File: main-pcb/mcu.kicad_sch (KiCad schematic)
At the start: 68 parts, among them J4 CORTEX_DEBUG_ETM, J5 CONN_01X03, U1 XC7S100-1FGGA484C, U12 AT24MAC402, U13 ECS-1612MV-250-CN, U14 STM32H735-UFBGA176-25, U15 S27KL0642GABHB020, U16 ECS-1612MV-250-CN

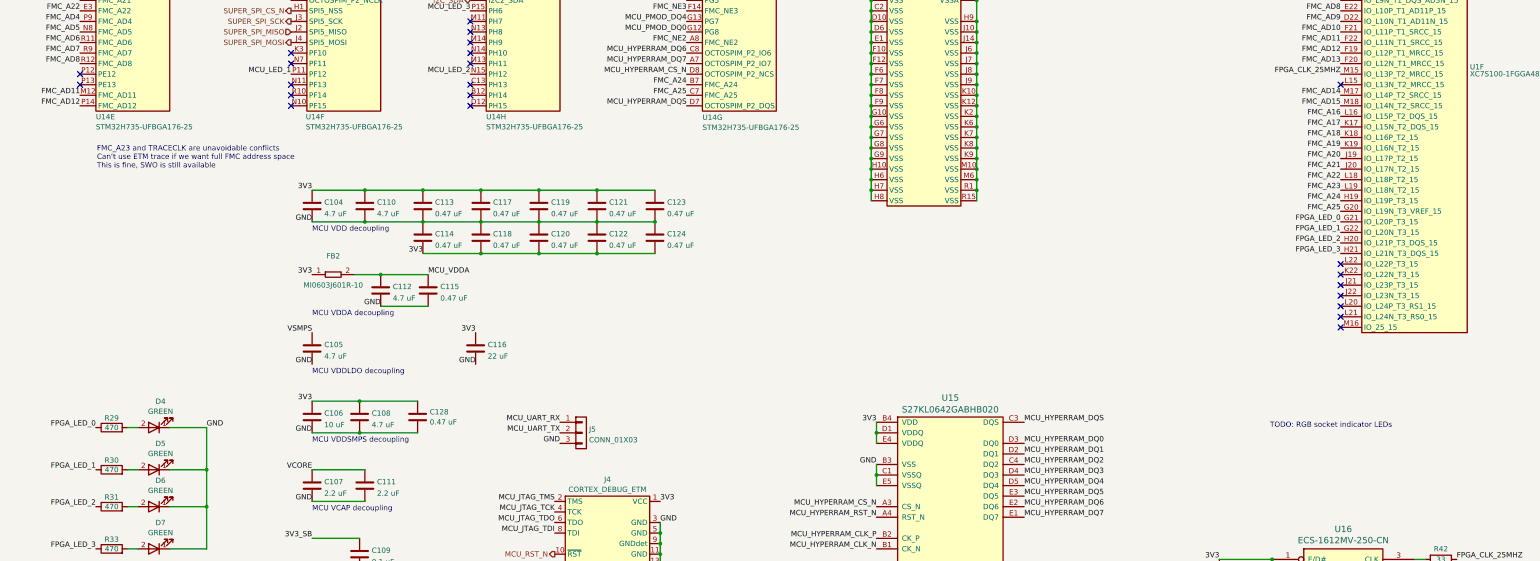
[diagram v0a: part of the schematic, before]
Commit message: Initial design mostly done aside from USB connector, review, test points
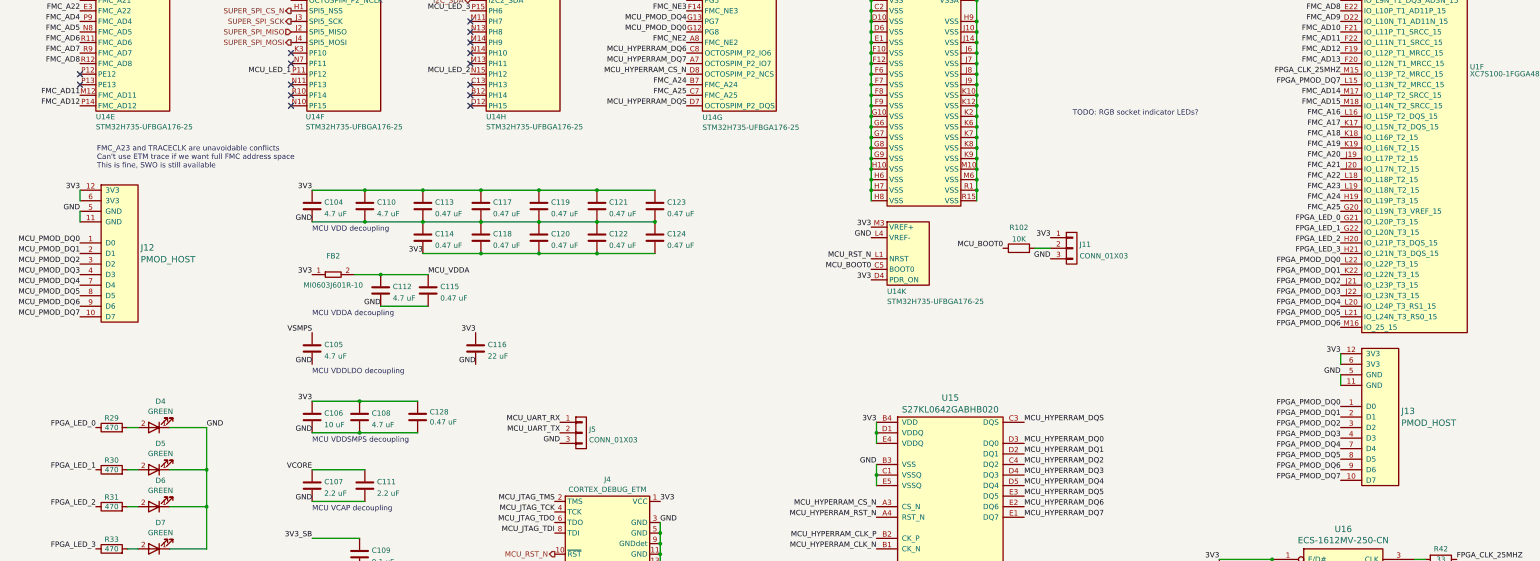
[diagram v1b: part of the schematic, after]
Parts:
- added J11: CONN_01X03, azonenberg_pcb:CONN_HEADER_2.54MM_1x3, symbol conn:CONN_01X03
- added J12, J13: PMOD_HOST, azonenberg_pcb:CONN_HEADER_2.54MM_2x6_RA_PMOD_HOST, symbol special-azonenberg:PMOD_HOST
- added R102: 10K, azonenberg_pcb:EIA_0402_RES_NOSILK, symbol device:R
- added unit 11 of U14
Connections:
- net 3V3: now also J11.1 (P1), J12.12 (3V3), J12.6 (3V3), J13.12 (3V3), J13.6 (3V3), U14.D4 (PDR_ON), U14.M3 (VREF+)
- net GND: now also J11.3 (P3), J12.11 (GND), J12.5 (GND), J13.11 (GND), J13.5 (GND), U14.L4 (VREF-)
- net MCU_PMOD_DQ0: now also J12.1 (D0)
- net MCU_PMOD_DQ1: now also J12.2 (D1)
- net MCU_PMOD_DQ2: now also J12.3 (D2)
- net MCU_PMOD_DQ3: now also J12.4 (D3)
- net MCU_PMOD_DQ4: now also J12.7 (D4)
- net MCU_PMOD_DQ5: now also J12.8 (D5)
- net MCU_PMOD_DQ6: now also J12.9 (D6)
- net MCU_PMOD_DQ7: now also J12.10 (D7)
- net MCU_RST_N: now also U14.L1 (NRST)
- net FPGA_PMOD_DQ2: now reaches U1.J21 (IO_L23P_T3_15)
- net FPGA_PMOD_DQ2: now also J13.3 (D2)
- net FPGA_PMOD_DQ3: now reaches U1.J22 (IO_L23N_T3_15)
- net FPGA_PMOD_DQ3: now also J13.4 (D3)
- net FPGA_PMOD_DQ1: now reaches U1.K22 (IO_L22N_T3_15)
- net FPGA_PMOD_DQ1: now also J13.2 (D1)
- net FPGA_PMOD_DQ7: now reaches U1.L15 (IO_L13N_T2_MRCC_15)
- net FPGA_PMOD_DQ7: now also J13.10 (D7)
- net FPGA_PMOD_DQ4: now reaches U1.L20 (IO_L24P_T3_RS1_15)
- net FPGA_PMOD_DQ4: now also J13.7 (D4)
- net FPGA_PMOD_DQ5: now reaches U1.L21 (IO_L24N_T3_RS0_15)
- net FPGA_PMOD_DQ5: now also J13.8 (D5)
- net FPGA_PMOD_DQ0: now reaches U1.L22 (IO_L22P_T3_15)
- net FPGA_PMOD_DQ0: now also J13.1 (D0)
- net FPGA_PMOD_DQ6: now reaches U1.M16 (IO_25_15)
- net FPGA_PMOD_DQ6: now also J13.9 (D6)
- new net: J11.2 (P2), R102.2
- new net MCU_BOOT0: R102.1, U14.C5 (BOOT0)
- no-connect marks 68 -> 60
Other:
- note added: "TODO: RGB socket indicator LEDs?"
- note removed: "TODO: RGB socket indicator LEDs"

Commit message: Finished initial schematic pass, ready for review
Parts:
- added R107: 10K, symbol device:R
- added TP17: CONN_01X03, azonenberg_pcb:CONN_HEADER_2.54MM_1x3, symbol conn:CONN_01X03
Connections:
- net 3V3: now also R41.1, R107.1
- net GND: now also TP17.3 (P3); no longer R41.1
- net I2C_SCL: now also TP17.2 (P2)
- net I2C_SDA: now also TP17.1 (P1)
- net MCU_HYPERRAM_RST_N: now also R107.2
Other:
- moved on the sheet: J5
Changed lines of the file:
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@@
 	)
 	(junction
+		(at 241.3 262.89)
+		(diameter 0)
+		(color 0 0 0 0)
+	)
+	(junction
 		(at 118.11 144.78)
 		(diameter 0)
@@
 	(wire
 		(pts
+			(xy 241.3 262.89) (xy 269.24 262.89)
+		)
+		(stroke
+			(width 0)
+			(type default)
+		)
+	)
+	(wire
+		(pts
 			(xy 240.03 64.77) (xy 240.03 67.31)
 		)
@@
 		)
 	)
+	(label "I2C_SCL"
+		(at 180.34 190.5 180)
+		(fields_autoplaced yes)
+		(effects
+			(font
+				(size 1.27 1.27)
+			)
+			(justify right bottom)
+		)
+	)
 	(label "FMC_A18"
 		(at 353.06 132.08 180)
@@
 		)
 	)
-	(label "GND"
+	(label "3V3"
 		(at 238.76 262.89 180)
 		(fields_autoplaced yes)
@@
 	)
 	(label "GND"
-		(at 165.1 205.74 180)
+		(at 180.34 203.2 180)
 		(fields_autoplaced yes)
 		(effects
@@
 		)
 	)
+	(label "I2C_SDA"
+		(at 180.34 187.96 180)
+		(fields_autoplaced yes)
+		(effects
+			(font
+				(size 1.27 1.27)
+			)
+			(justify right bottom)
+		)
+	)
 	(label "MCU_HYPERRAM_DQ5"
 		(at 195.58 88.9 180)
@@
 	)
 	(label "MCU_UART_RX"
-		(at 165.1 200.66 180)
+		(at 180.34 198.12 180)
 		(fields_autoplaced yes)
 		(effects
@@
 		)
 	)
+	(label "GND"
+		(at 180.34 193.04 180)
+		(fields_autoplaced yes)
+		(effects
+			(font
+				(size 1.27 1.27)
+			)
+			(justify right bottom)
+		)
+	)
 	(label "MCU_HYPERRAM_DQ3"
 		(at 276.86 213.36 0)
@@
 	)
 	(label "MCU_UART_TX"
-		(at 165.1 203.2 180)
+		(at 180.34 200.66 180)
 		(fields_autoplaced yes)
 		(effects
@@
 		)
 	)
+	(label "MCU_HYPERRAM_RST_N"
+		(at 269.24 255.27 180)
+		(fields_autoplaced yes)
+		(effects
+			(font
+				(size 1.27 1.27)
+			)
+			(justify right bottom)
+		)
+	)
 	(label "MCU_UART_TX"
 		(at 49.53 62.23 180)
@@
 	)
 	(symbol
+		(lib_id "conn:CONN_01X03")
+		(at 185.42 190.5 0)
+		(unit 1)
+		(exclude_from_sim no)
+		(in_bom yes)
+		(on_board yes)
+		(dnp no)
+		(fields_autoplaced yes)
+		(property "Reference" "TP17"
+			(at 187.325 189.2878 0)
+			(effects
+				(font
+					(size 1.27 1.27)
+				)
+				(justify left)
+			)
+		)
+		(property "Value" "CONN_01X03"
+			(at 187.325 191.7121 0)
+			(effects
+				(font
+					(size 1.27 1.27)
+				)
+				(justify left)
+			)
+		)
+		(property "Footprint" "azonenberg_pcb:CONN_HEADER_2.54MM_1x3"
+			(at 185.42 190.5 0)
+			(effects
+				(font
+					(size 1.27 1.27)
+				)
+				(hide yes)
+			)
+		)
+		(property "Datasheet" ""
+			(at 185.42 190.5 0)
+			(effects
+				(font
+					(size 1.27 1.27)
+				)
+				(hide yes)
+			)
+		)
+		(property "Description" ""
+			(at 185.42 190.5 0)
+			(effects
+				(font
+					(size 1.27 1.27)
+				)
+				(hide yes)
+			)
+		)
+		(pin "1"
+		)
+		(pin "2"
+		)
+		(pin "3"
+		)
+		(instances
+			(project "main-pcb"
+				(path "/e33e9f2b-a48c-455d-96ec-c7304b1720d3/06fb2b2f-cee1-4298-9f6c-0918538b690d"
+					(reference "TP17")
+					(unit 1)
+				)
+			)
+		)
+	)
+	(symbol
 		(lib_id "device:LED")
 		(at 67.31 201.93 180)
@@
 	)
 	(symbol
+		(lib_id "device:R")
+		(at 269.24 259.08 180)
+		(unit 1)
+		(exclude_from_sim no)
+		(in_bom yes)
+		(on_board yes)
+		(dnp no)
+		(fields_autoplaced yes)
+		(property "Reference" "R107"
+			(at 271.018 257.8678 0)
+			(effects
+				(font
+					(size 1.27 1.27)
+				)
+				(justify right)
+			)
+		)
+		(property "Value" "10K"
+			(at 271.018 260.2921 0)
+			(effects
+				(font
+					(size 1.27 1.27)
+				)
+				(justify right)
+			)
+		)
+		(property "Footprint" ""
+			(at 271.018 259.08 90)
+			(effects
+				(font
+					(size 1.27 1.27)
+				)
+				(hide yes)
+			)
+		)
+		(property "Datasheet" ""
+			(at 269.24 259.08 0)
+			(effects
+				(font
+					(size 1.27 1.27)
+				)
+				(hide yes)
+			)
+		)
+		(property "Description" "Resistor"
+			(at 269.24 259.08 0)
+			(effects
+				(font
+					(size 1.27 1.27)
+				)
+				(hide yes)
+			)
+		)
+		(pin "2"
+		)
+		(pin "1"
+		)
+		(instances
+			(project "main-pcb"
+				(path "/e33e9f2b-a48c-455d-96ec-c7304b1720d3/06fb2b2f-cee1-4298-9f6c-0918538b690d"
+					(reference "R107")
+					(unit 1)
+				)
+			)
+		)
+	)
+	(symbol
 		(lib_id "device:C")
 		(at 121.92 168.91 0)
@@
 	(symbol
 		(lib_id "conn:CONN_01X03")
-		(at 170.18 203.2 0)
+		(at 185.42 200.66 0)
 		(unit 1)
 		(exclude_from_sim no)
@@
 		(fields_autoplaced yes)
 		(property "Reference" "J5"
-			(at 172.085 202.3653 0)
+			(at 187.325 199.8253 0)
 			(effects
 				(font
@@
 		)
 		(property "Value" "CONN_01X03"
-			(at 172.085 204.9022 0)
+			(at 187.325 202.3622 0)
 			(effects
 				(font
@@
 		)
 		(property "Footprint" "azonenberg_pcb:CONN_HEADER_2.54MM_1x3"
-			(at 170.18 203.2 0)
+			(at 185.42 200.66 0)
 			(effects
 				(font
@@
 		)
 		(property "Datasheet" ""
-			(at 170.18 203.2 0)
+			(at 185.42 200.66 0)
 			(effects
 				(font
@@
 		)
 		(property "Description" ""
-			(at 170.18 203.2 0)
+			(at 185.42 200.66 0)
 			(effects
 				(font

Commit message: More schematic tweaks and test points
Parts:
- C129: footprint (none) -> azonenberg_pcb:EIA_0603_CAP_NOSILK
- C130, C131, C132: footprint (none) -> azonenberg_pcb:EIA_0402_CAP_NOSILK
- D10, D11, D4, D5, D6, D7, D8, D9: footprint (none) -> azonenberg_pcb:EIA_0402_LED
- R107, R41: footprint (none) -> azonenberg_pcb:EIA_0402_RES_NOSILK
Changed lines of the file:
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@@
 			)
 		)
-		(property "Footprint" ""
+		(property "Footprint" "azonenberg_pcb:EIA_0402_LED"
 			(at 67.31 201.93 0)
 			(effects
@@
 			)
 		)
-		(property "Footprint" ""
+		(property "Footprint" "azonenberg_pcb:EIA_0402_LED"
 			(at 67.31 231.14 0)
 			(effects
@@
 			)
 		)
-		(property "Footprint" ""
+		(property "Footprint" "azonenberg_pcb:EIA_0402_CAP_NOSILK"
 			(at 287.9852 250.19 0)
 			(effects
@@
 			)
 		)
-		(property "Footprint" ""
+		(property "Footprint" "azonenberg_pcb:EIA_0402_RES_NOSILK"
 			(at 271.018 259.08 90)
 			(effects
@@
 			)
 		)
-		(property "Footprint" ""
+		(property "Footprint" "azonenberg_pcb:EIA_0603_CAP_NOSILK"
 			(at 247.3452 250.19 0)
 			(effects
@@
 			)
 		)
-		(property "Footprint" ""
+		(property "Footprint" "azonenberg_pcb:EIA_0402_LED"
 			(at 67.31 254 0)
 			(effects
@@
 			)
 		)
-		(property "Footprint" ""
+		(property "Footprint" "azonenberg_pcb:EIA_0402_CAP_NOSILK"
 			(at 260.0452 250.19 0)
 			(effects
@@
 			)
 		)
-		(property "Footprint" ""
+		(property "Footprint" "azonenberg_pcb:EIA_0402_CAP_NOSILK"
 			(at 274.0152 250.19 0)
 			(effects
@@
 			)
 		)
-		(property "Footprint" ""
+		(property "Footprint" "azonenberg_pcb:EIA_0402_LED"
 			(at 67.31 212.09 0)
 			(effects
@@
 			)
 		)
-		(property "Footprint" ""
+		(property "Footprint" "azonenberg_pcb:EIA_0402_LED"
 			(at 67.31 273.05 0)
 			(effects
@@
 			)
 		)
-		(property "Footprint" ""
+		(property "Footprint" "azonenberg_pcb:EIA_0402_LED"
 			(at 67.31 243.84 0)
 			(effects
@@
 			)
 		)
-		(property "Footprint" ""
+		(property "Footprint" "azonenberg_pcb:EIA_0402_RES_NOSILK"
 			(at 243.078 259.08 90)
 			(effects
@@
 			)
 		)
-		(property "Footprint" ""
+		(property "Footprint" "azonenberg_pcb:EIA_0402_LED"
 			(at 67.31 262.89 0)
 			(effects
@@
 			)
 		)
-		(property "Footprint" ""
+		(property "Footprint" "azonenberg_pcb:EIA_0402_LED"
 			(at 67.31 220.98 0)
 			(effects

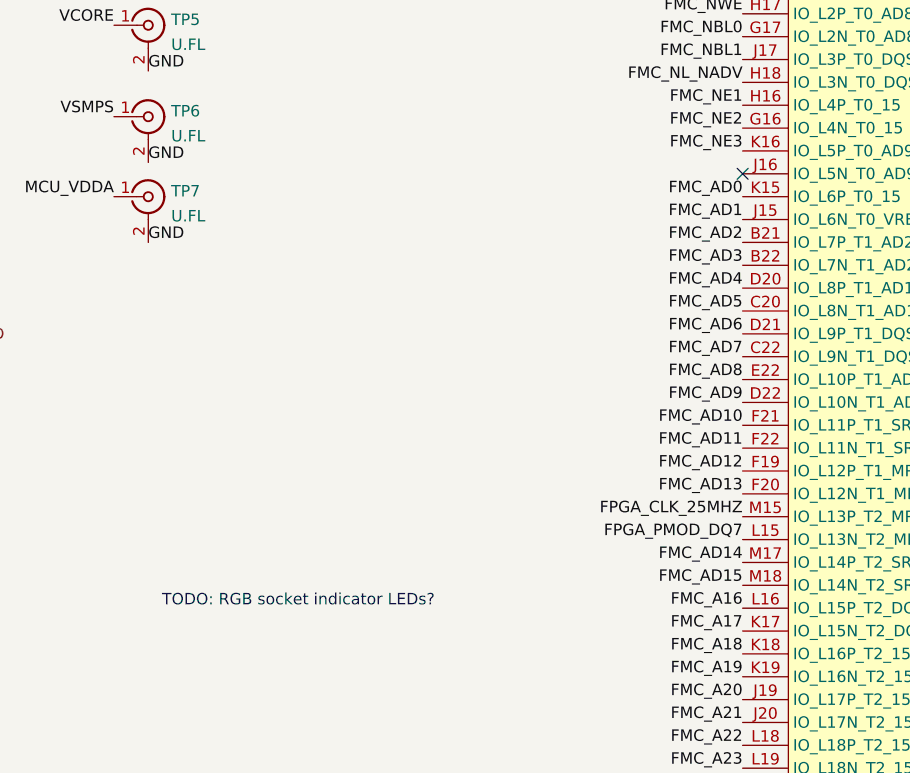
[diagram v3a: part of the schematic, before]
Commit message: Added some RGB LEDs, changed a few voltage dividers to match what was in stock. Time for next round of review.
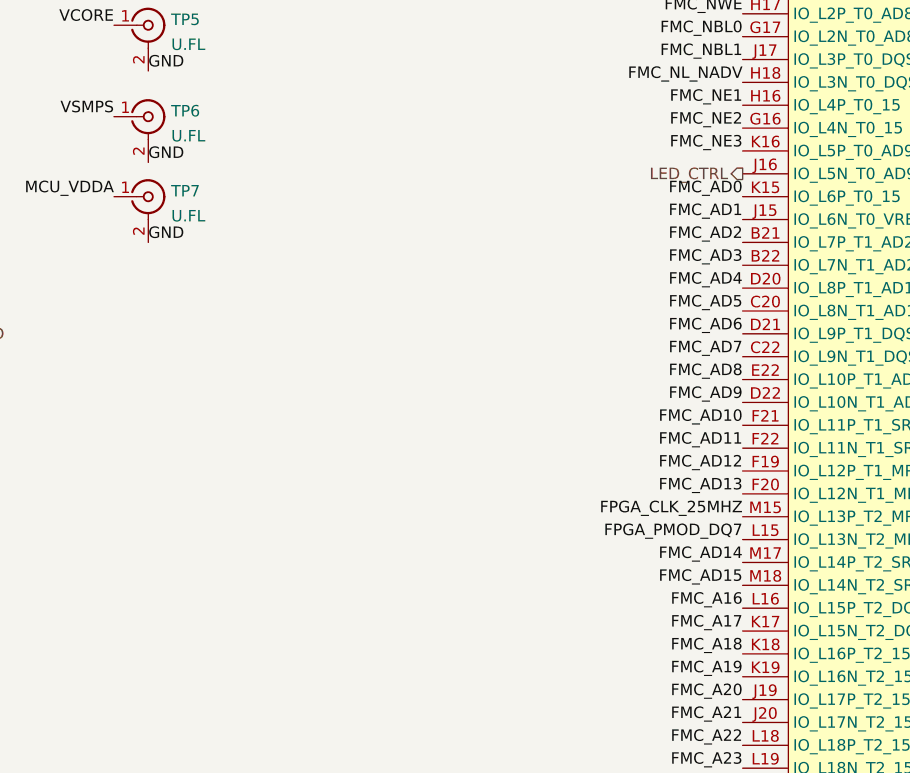
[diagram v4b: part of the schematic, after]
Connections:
- net LED_CTRL: now reaches U1.J16 (IO_L5N_T0_AD9N_15)
- no-connect marks 60 -> 59
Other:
- note removed: "TODO: RGB socket indicator LEDs?"
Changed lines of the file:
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@@
 	(title_block
 		(title "DUMPTRUCK flash dumper")
-		(date "2024-10-16")
+		(date "2024-10-17")
 		(rev "0.1")
 		(company "Antikernel Labs")
@@
 	)
 	(no_connect
-		(at 353.06 78.74)
-	)
-	(no_connect
 		(at 100.33 119.38)
 	)
@@
 		)
 	)
-	(text "TODO: RGB socket indicator LEDs?"
-		(exclude_from_sim no)
-		(at 288.544 126.238 0)
-		(effects
-			(font
-				(size 1.27 1.27)
-			)
-			(justify left)
-		)
-	)
 	(text "MCU VDD decoupling"
 		(exclude_from_sim no)
@@
 		(fields_autoplaced yes)
 		(effects
+			(font
+				(size 1.27 1.27)
+			)
+			(justify right)
+		)
+	)
+	(hierarchical_label "LED_CTRL"
+		(shape output)
+		(at 353.06 78.74 180)
+		(fields_autoplaced yes)
+		(effects

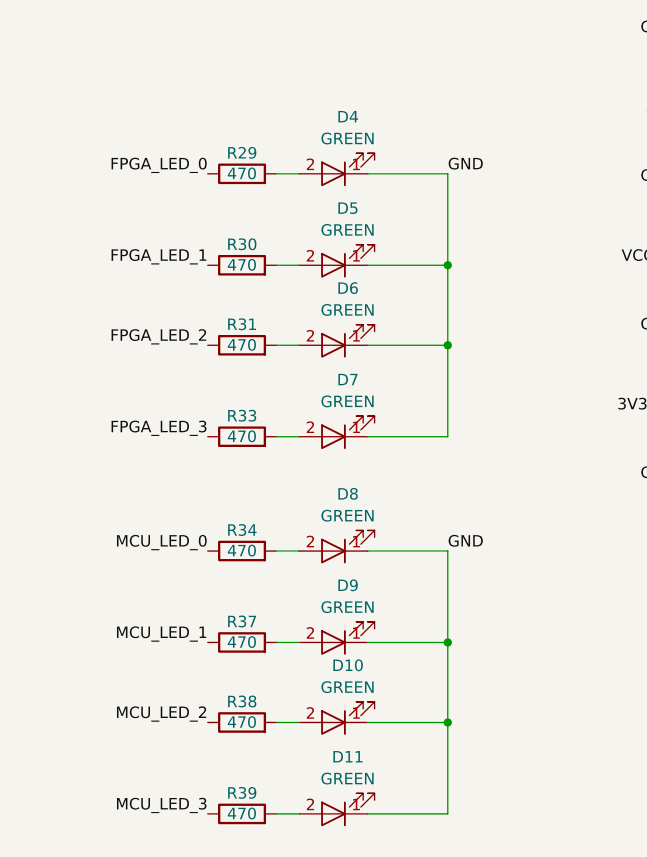
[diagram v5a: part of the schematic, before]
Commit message: Continued layout mostly of DUT connectors
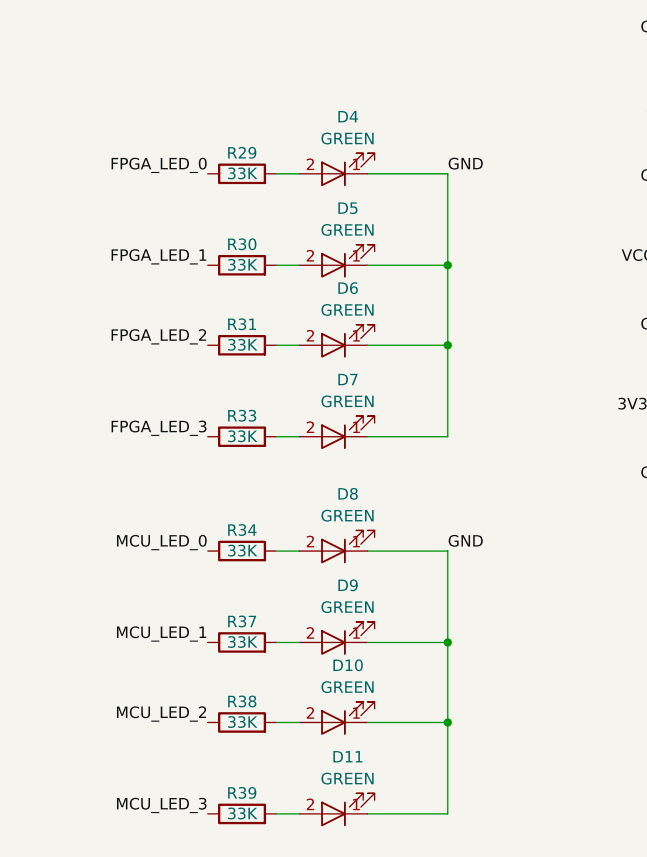
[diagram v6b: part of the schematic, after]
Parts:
- R29, R30, R31, R33, R34, R37, R38, R39: value 470 -> 33K
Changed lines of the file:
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@@
 	(title_block
 		(title "DUMPTRUCK flash dumper")
-		(date "2024-10-18")
+		(date "2024-10-19")
 		(rev "0.1")
 		(company "Antikernel Labs")
@@
 			)
 		)
-		(property "Value" "470"
+		(property "Value" "33K"
 			(at 57.15 212.09 90)
 			(effects
@@
 			)
 		)
-		(property "Value" "470"
+		(property "Value" "33K"
 			(at 57.15 201.93 90)
 			(effects
@@
 			)
 		)
-		(property "Value" "470"
+		(property "Value" "33K"
 			(at 57.15 231.14 90)
 			(effects
@@
 			)
 		)
-		(property "Value" "470"
+		(property "Value" "33K"
 			(at 57.15 243.84 90)
 			(effects
@@
 			)
 		)
-		(property "Value" "470"
+		(property "Value" "33K"
 			(at 57.15 220.98 90)
 			(effects
@@
 			)
 		)
-		(property "Value" "470"
+		(property "Value" "33K"
 			(at 57.15 273.05 90)
 			(effects
@@
 			)
 		)
-		(property "Value" "470"
+		(property "Value" "33K"
 			(at 57.15 262.89 90)
 			(effects
@@
 			)
 		)
-		(property "Value" "470"
+		(property "Value" "33K"
 			(at 57.15 254 90)
 			(effects
